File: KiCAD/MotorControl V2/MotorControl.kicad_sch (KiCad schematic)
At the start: 17 parts, among them M1 Motor_DC, U1 LM324, U2 LM324, U3 LM324, U4 OPA548FKTWT

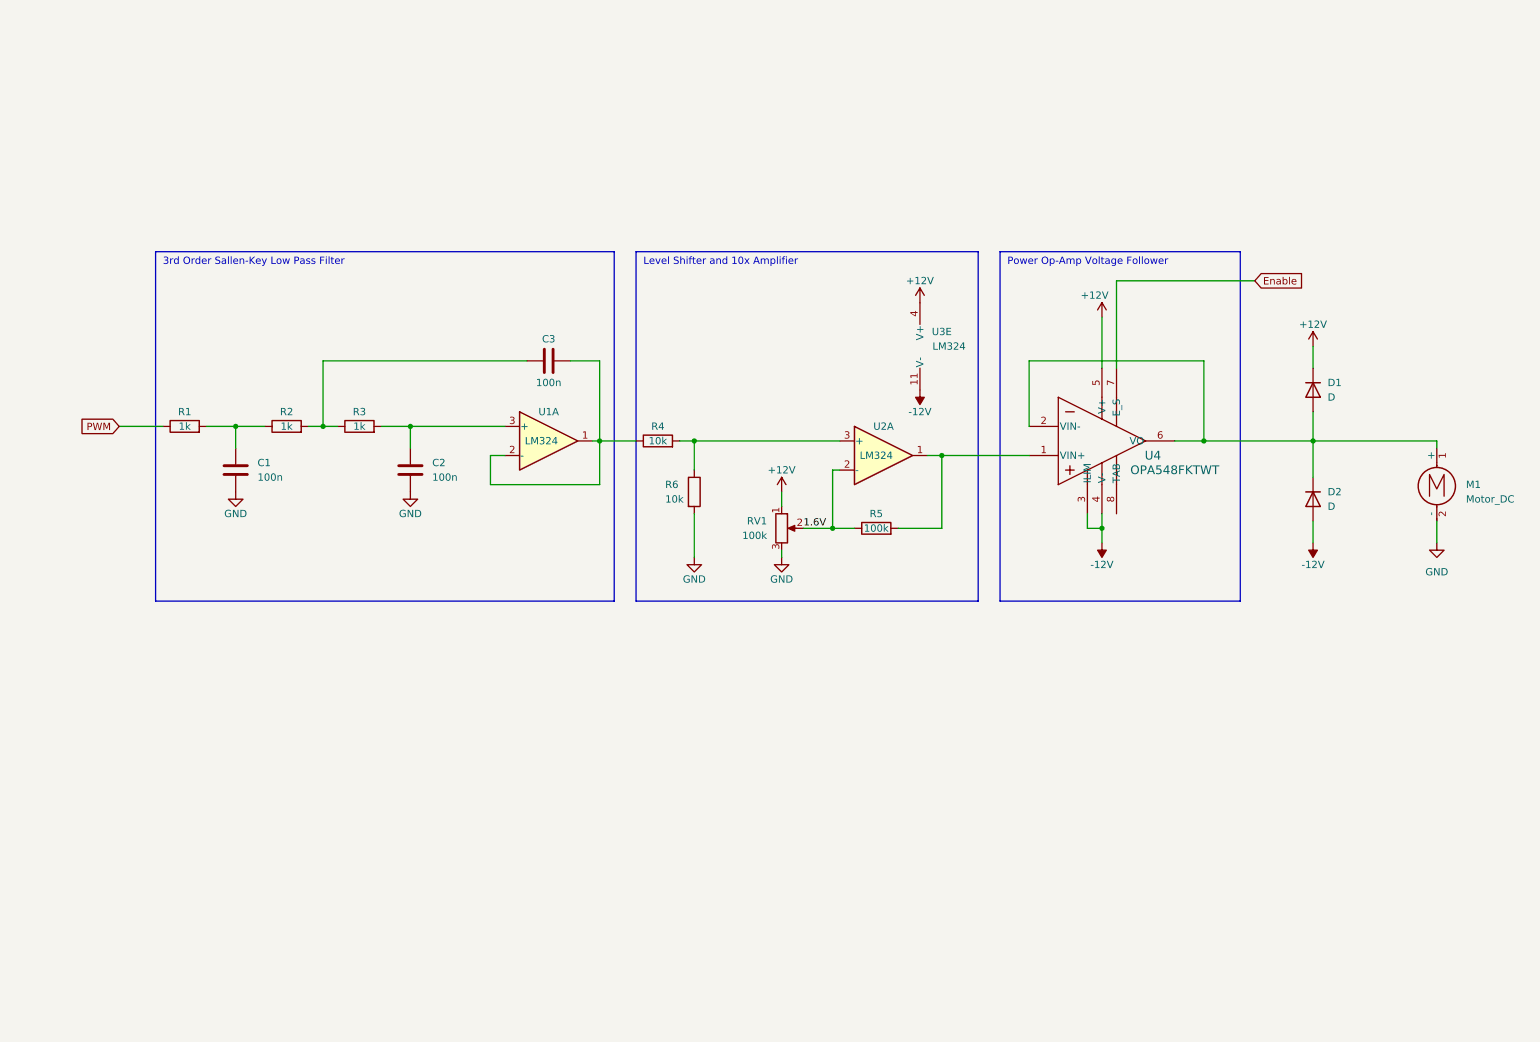
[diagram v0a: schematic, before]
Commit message: adds enable circuit
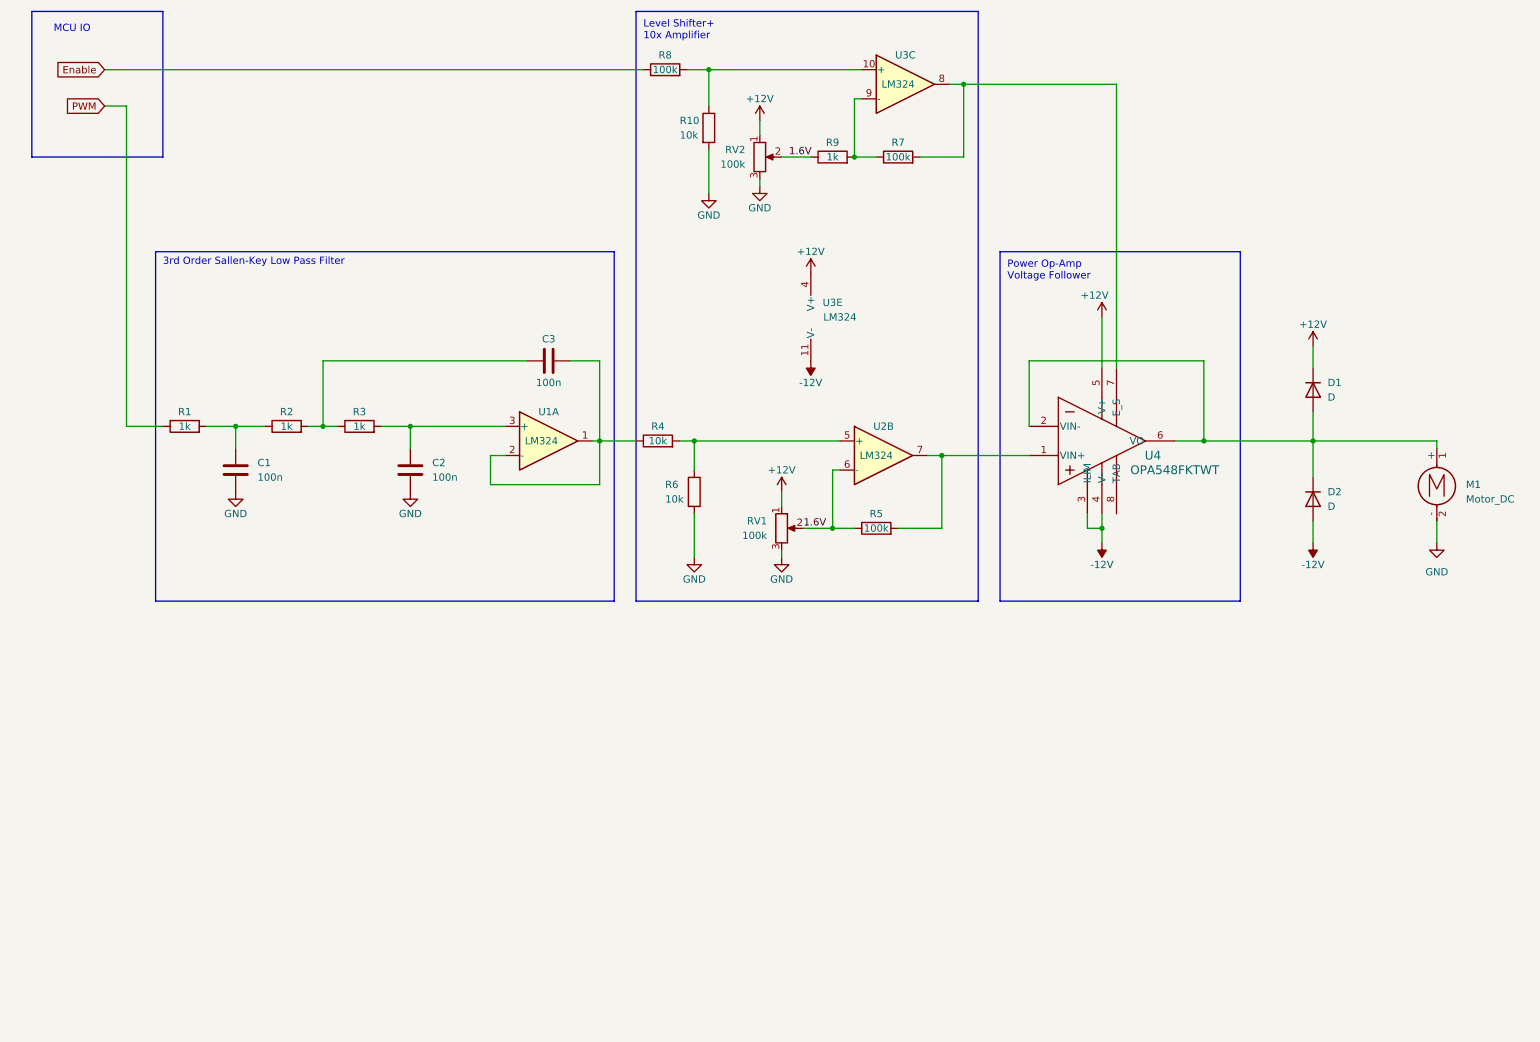
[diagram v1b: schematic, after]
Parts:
- added R10: 10k, symbol Device:R
- added R7, R8: 100k, symbol Device:R
- added R9: 1k, symbol Device:R
- added RV2: 100k, symbol Device:R_Potentiometer
- added unit 3 of U3
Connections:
- net +12V: now also RV2.1
- net 1.6V: now also U2.6 (-), R9.1, RV2.2; no longer U2.2 (-)
- net Enable: now also R8.1; no longer U4.7 (E_S)
- net GND: now also R10.2, RV2.3
- net at R4.2, R6.1: now also U2.5 (+); no longer U2.3 (+)
- net at R5.2, U4.1 (VIN+): now also U2.7; no longer U2.1
- new net: R7.1, R9.2, U3.9 (-)
- new net: R10.1, R8.2, U3.10 (+)
- new net: R7.2, U3.8, U4.7 (E_S)
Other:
- note added: "Level Shifter+ 10x Amplifier"
- note added: "MCU IO"
- note removed: "Level Shifter and 10x Amplifier"
- moved on the sheet: U3E

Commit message: sync
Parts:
- added D3: ~, LED_THT:LED_D3.0mm_IRBlack, symbol LED:IR204A
- added Q1: ~, LED_THT:LED_D3.0mm_Clear, symbol Sensor_Optical:BPW85A
- added R11: 10k, symbol Device:R
- added R12: 1k, symbol Device:R
- added U5: L7805, symbol Regulator_Linear:L7805
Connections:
- net +12V: now also U5.1 (IN)
- net GND: now also Q1.2 (E), R12.2, U5.2 (GND)
- new net: D3.1 (K), R12.1
- new net: D3.2 (A), R11.1, U5.3 (OUT)
- new net Encoder_BitX: Q1.1 (C), R11.2
- no-connect marks 0 -> 1
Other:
- note added: "IR Sensor X 8"

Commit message: improving circuit
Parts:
- added D4, D5: D, symbol Device:D
- added R13, R19: 1k, symbol Device:R
- added R14, R15, R16, R17: 100k, symbol Device:R
- added R18: 5k, symbol Device:R
- added R20, R21: 10k, symbol Device:R
- added RV3: 1k, symbol Device:R_Potentiometer
- added unit 4 of U1
- R10, R6: value 10k -> 100k
- R8: value 100k -> 10k
- R9: value 1k -> 10k
- RV1, RV2: value 100k -> 1k
- renumbered U3 to U1, U2 to U1
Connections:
- net -12V: now also RV3.3
- net 1.6V: no longer R5.1, RV1.2, U1.6 (-)
- net GND: now also D5.2 (A), R17.2, R19.2, RV3.1
- net at D1.2 (A), D2.1 (K), M1.1 (+)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: now also R13.2, R18.1; no longer U4.2 (VIN-)
- new net: R14.1, R15.2, U1.13 (-)
- new net: R14.2, RV3.2
- new net: R16.2, R17.1, R18.2, R19.1
- new net: R20.1, RV1.2
- new net: R16.1, U1.12 (+)
- new net: R15.1, R21.2, U1.14
- new net: R13.1, U4.2 (VIN-)
- new net: R20.2, R5.1, U1.6 (-)
- new net 3.3V: D4.1 (K)
- new net VoltageFeedback: D4.2 (A), D5.1 (K), R21.1
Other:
- note added: "Clipper Circuit"
- moved on the sheet: D3, Q1, R11, R12, RV1, U5

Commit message: update circuits
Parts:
- removed R18: 5k, symbol Device:R
- R19: value 1k -> 100k
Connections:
- net at D1.2 (A), D2.1 (K), M1.1 (+)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: now also R16.2, R17.1, R19.1
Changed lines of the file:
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@@
-    (stroke (width 0) (type default))
-  )
-  (wire (pts (xy 251.46 114.3) (xy 251.46 130.81))
     (stroke (width 0) (type default))
   )
@@
     (stroke (width 0) (type default))
   )
-  (wire (pts (xy 251.46 106.68) (xy 251.46 88.9))
+  (wire (pts (xy 251.46 88.9) (xy 251.46 130.81))
     (stroke (width 0) (type default))
   )
@@
     )
   )
-  (symbol (lib_id "Device:R") (at 251.46 110.49 0) (unit 1)
-    (in_bom yes) (on_board yes) (dnp no)
-    (property "Reference" "R18" (at 246.38 109.22 0)
-      (effects (font (size 1.27 1.27)) (justify left))
-    )
-    (property "Value" "5k" (at 247.65 111.76 0)
-      (effects (font (size 1.27 1.27)) (justify left))
-    )
-    (property "Footprint" "" (at 249.682 110.49 90)
-      (effects (font (size 1.27 1.27)) hide)
-    )
-    (property "Datasheet" "~" (at 251.46 110.49 0)
-      (effects (font (size 1.27 1.27)) hide)
-    )
-    (pin "1")
-    (pin "2")
-    (instances
-      (project "MotorControl"
-        (path "/f9a38581-22a3-459c-b39f-09f02d27a2a1"
-          (reference "R18") (unit 1)
-        )
-      )
-    )
-  )
   (symbol (lib_id "Device:R") (at 125.73 88.9 90) (unit 1)
     (in_bom yes) (on_board yes) (dnp no)
@@
       (effects (font (size 1.27 1.27)) (justify left))
     )
-    (property "Value" "1k" (at 247.65 140.97 0)
-      (effects (font (size 1.27 1.27)) (justify left))
-    )
+    (property "Value" "100k" (at 245.11 140.97 0)
+      (effects (font (size 1.27 1.27)) (justify left))
+    )
